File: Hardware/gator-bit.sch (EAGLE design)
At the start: 76 parts, among them J19 GATOR, J2 GATOR, J20 GATOR, J21 GATOR, J22 GATOR, J25 GATOR, J28 GATOR, J3 GATOR, J32 GATOR, J33 GATOR, J34 GATOR, J35 GATOR, J36 GATOR, J39 GATOR, J4 GATOR, J40 GATOR, U1 TPS63070, U2 micro:bit

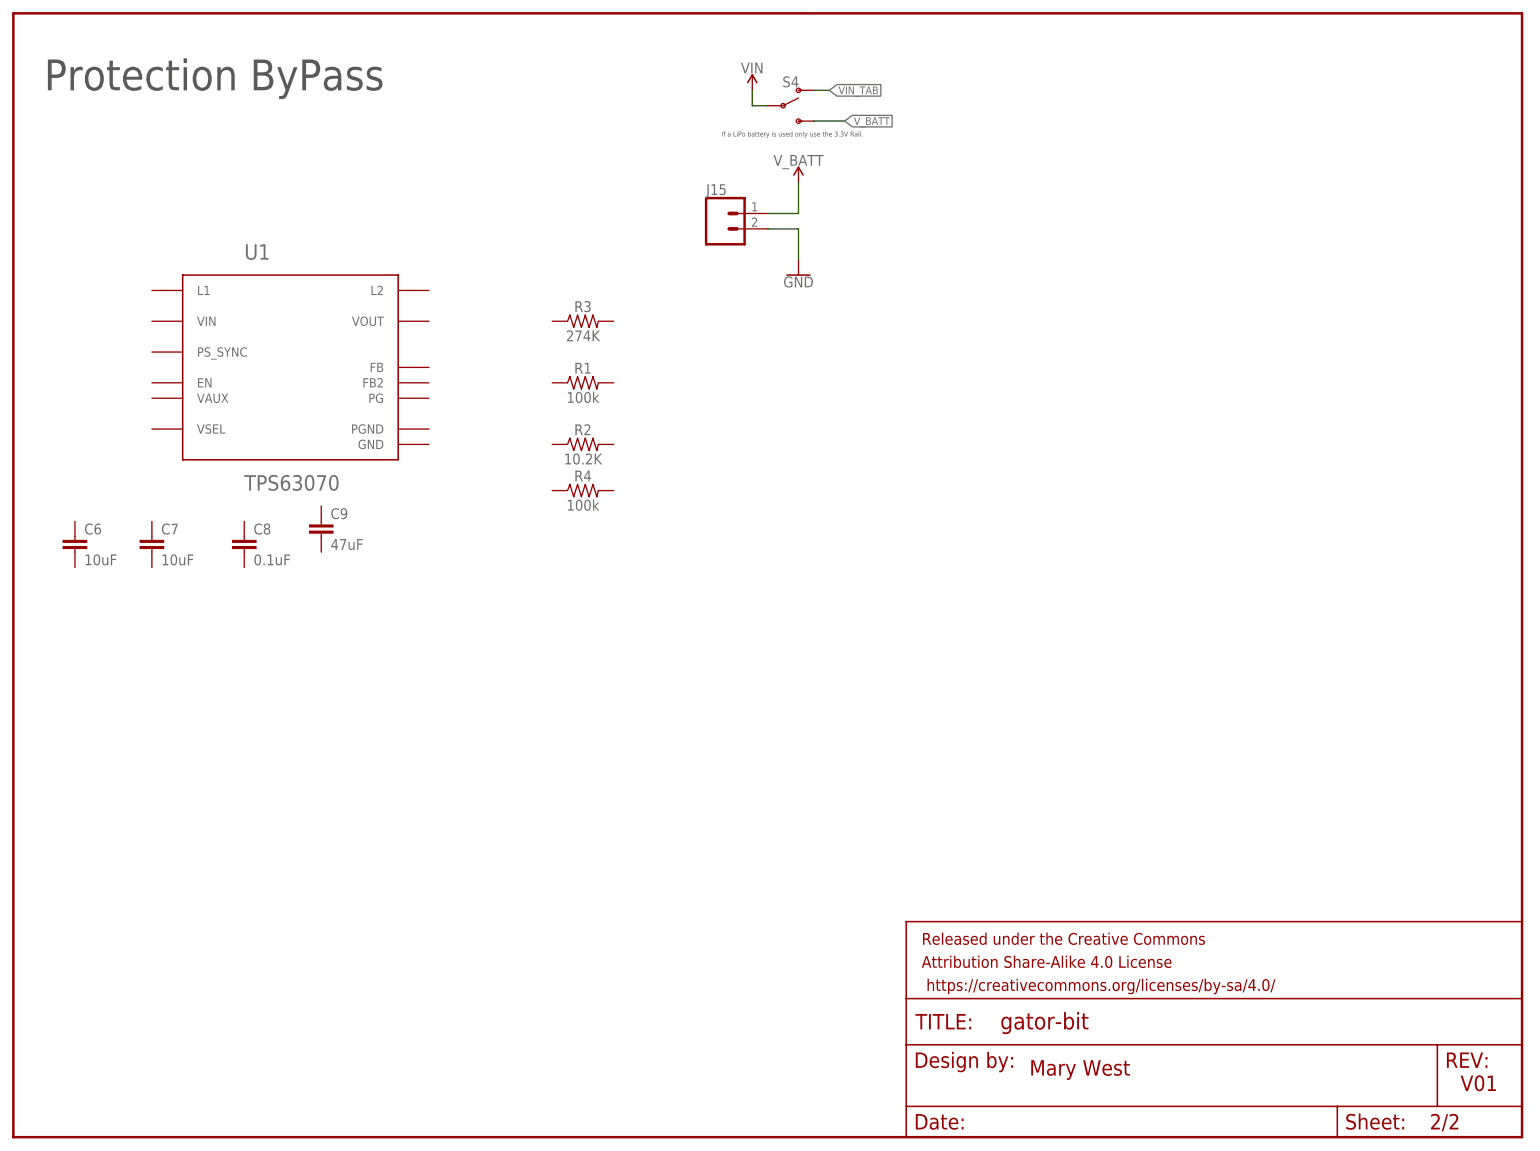
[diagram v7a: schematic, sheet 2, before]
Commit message: Added Inductor
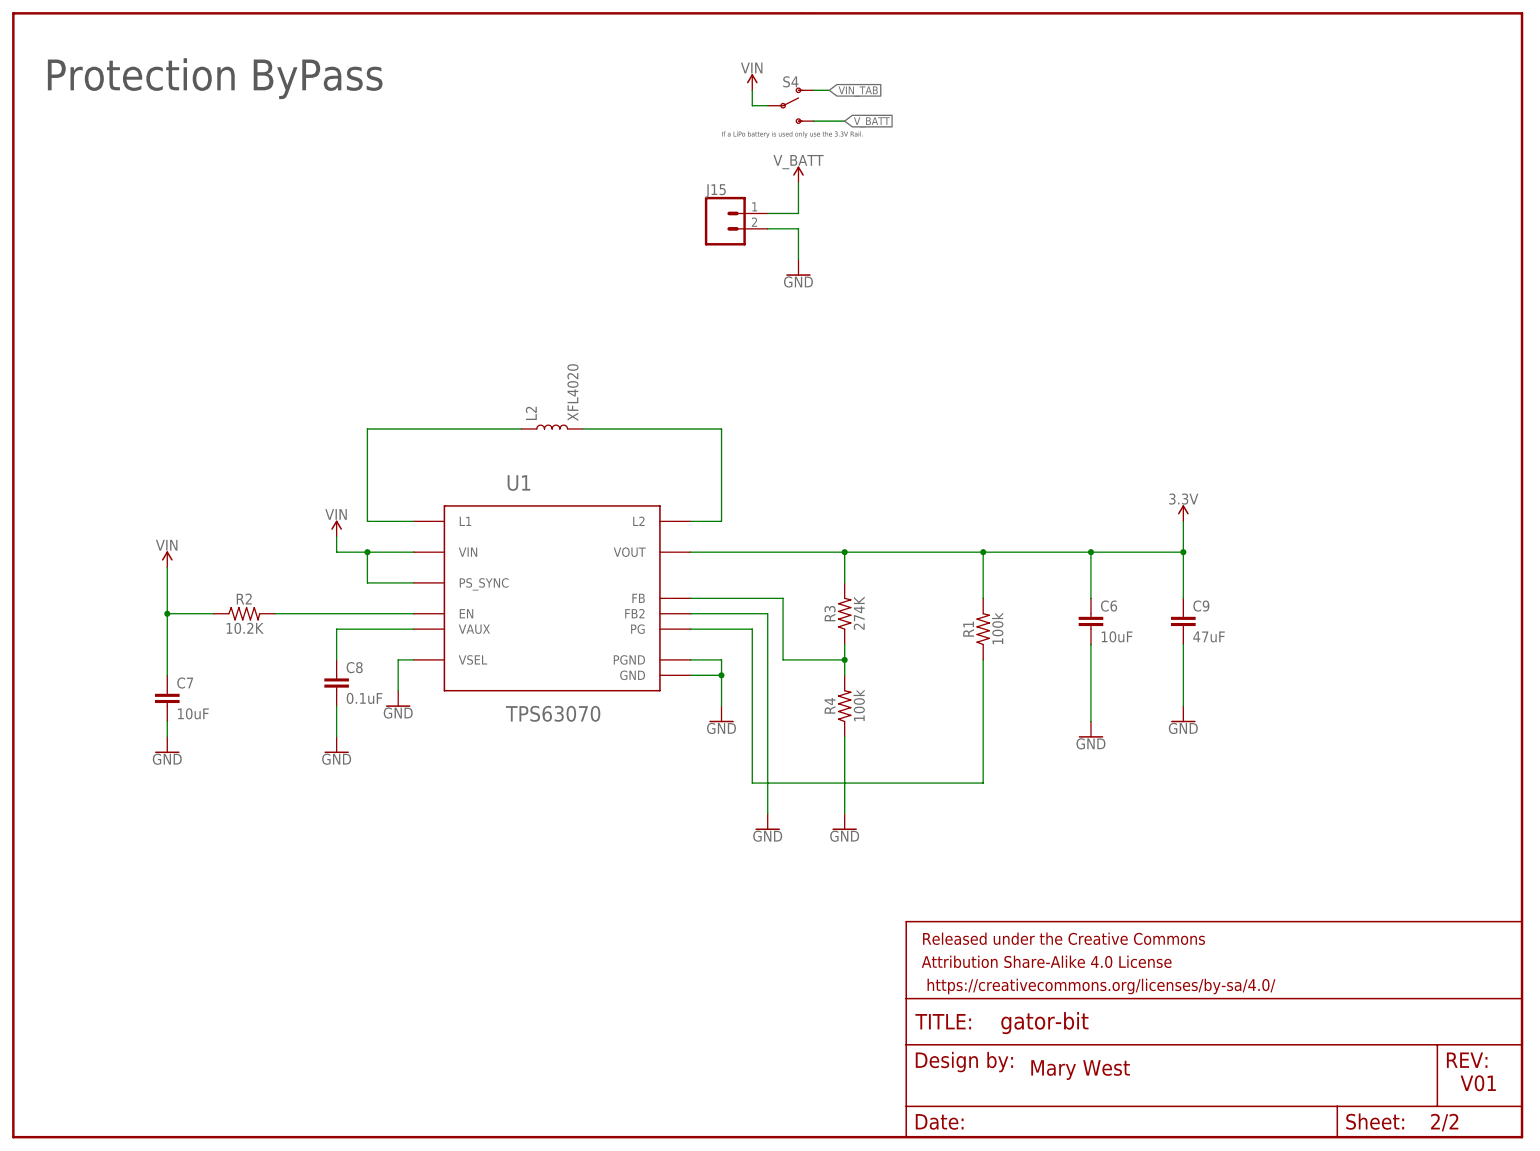
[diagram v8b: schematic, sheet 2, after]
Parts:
- added L2: XFL4020, SparkFun-Coils:XFL4020
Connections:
- new net N$11: R3.1, R4.2, U1.FB
- new net N$12: C8.1, U1.VAUX
- new net N$13: R2.2, U1.EN
- new net N$14: R1.1, U1.PG
- new net N$2: L2.1, U1.L1
- new net N$8: L2.2, U1.L2
- net 3.3V: now also C6.1, C9.1, R1.2, R3.2, U1.VOUT
- net GND: now also C6.2, C7.2, C8.2, C9.2, R4.1, U1.FB2, U1.GND, U1.PGND, U1.VSEL
- net VIN: now also C7.1, R2.1, U1.PS_SYNC, U1.VIN
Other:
- moved on the sheet: C6, C7, C8, C9, R1, R2, R3, R4, U1
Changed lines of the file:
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@@
 <part name="C8" library="SparkFun-Capacitors" deviceset="0.1UF" device="-0603-25V-(+80/-20%)" value="0.1uF"/>
 <part name="C9" library="SparkFun-Capacitors" deviceset="47UF" device="" technology="20%-6.3V-0805" value="47uF"/>
+<part name="L2" library="SparkFun-Coils" deviceset="XFL4020" device=""/>
+<part name="GND7" library="SparkFun-PowerSymbols" deviceset="GND" device=""/>
+<part name="GND8" library="SparkFun-PowerSymbols" deviceset="GND" device=""/>
+<part name="GND9" library="SparkFun-PowerSymbols" deviceset="GND" device=""/>
+<part name="SUPPLY18" library="SparkFun-PowerSymbols" deviceset="VIN" device=""/>
+<part name="SUPPLY19" library="SparkFun-PowerSymbols" deviceset="VIN" device=""/>
+<part name="GND10" library="SparkFun-PowerSymbols" deviceset="GND" device=""/>
+<part name="GND11" library="SparkFun-PowerSymbols" deviceset="GND" device=""/>
+<part name="GND17" library="SparkFun-PowerSymbols" deviceset="GND" device=""/>
+<part name="GND18" library="SparkFun-PowerSymbols" deviceset="GND" device=""/>
+<part name="GND20" library="SparkFun-PowerSymbols" deviceset="GND" device=""/>
+<part name="SUPPLY20" library="SparkFun-PowerSymbols" deviceset="3.3V" device=""/>
 </parts>
 <sheets>
@@
 <instance part="S4" gate="1" x="127" y="170.18"/>
 <instance part="SUPPLY3" gate="G$1" x="121.92" y="172.72"/>
-<instance part="U1" gate="G$1" x="45.72" y="127"/>
-<instance part="R1" gate="G$1" x="93.98" y="124.46"/>
-<instance part="R2" gate="G$1" x="93.98" y="114.3"/>
-<instance part="R3" gate="G$1" x="93.98" y="134.62"/>
-<instance part="R4" gate="G$1" x="93.98" y="106.68"/>
-<instance part="C6" gate="G$1" x="10.16" y="96.52"/>
-<instance part="C7" gate="G$1" x="22.86" y="96.52"/>
-<instance part="C8" gate="G$1" x="38.1" y="96.52"/>
-<instance part="C9" gate="G$1" x="50.8" y="99.06"/>
+<instance part="U1" gate="G$1" x="88.9" y="88.9"/>
+<instance part="R1" gate="G$1" x="160.02" y="83.82" rot="R90"/>
+<instance part="R2" gate="G$1" x="38.1" y="86.36"/>
+<instance part="R3" gate="G$1" x="137.16" y="86.36" rot="R90"/>
+<instance part="R4" gate="G$1" x="137.16" y="71.12" rot="R90"/>
+<instance part="C6" gate="G$1" x="177.8" y="83.82"/>
+<instance part="C7" gate="G$1" x="25.4" y="71.12"/>
+<instance part="C8" gate="G$1" x="53.34" y="73.66"/>
+<instance part="C9" gate="G$1" x="193.04" y="83.82"/>
+<instance part="L2" gate="G$1" x="88.9" y="116.84" rot="R90"/>
+<instance part="GND7" gate="1" x="53.34" y="63.5"/>
+<instance part="GND8" gate="1" x="25.4" y="63.5"/>
+<instance part="GND9" gate="1" x="63.5" y="71.12"/>
+<instance part="SUPPLY18" gate="G$1" x="53.34" y="99.06"/>
+<instance part="SUPPLY19" gate="G$1" x="25.4" y="93.98"/>
+<instance part="GND10" gate="1" x="116.84" y="68.58"/>
+<instance part="GND11" gate="1" x="137.16" y="50.8"/>
+<instance part="GND17" gate="1" x="124.46" y="50.8"/>
+<instance part="GND18" gate="1" x="177.8" y="66.04"/>
+<instance part="GND20" gate="1" x="193.04" y="68.58"/>
+<instance part="SUPPLY20" gate="G$1" x="193.04" y="101.6"/>
 </instances>
 <busses>
@@
 <pinref part="GND26" gate="1" pin="GND"/>
 </segment>
+<segment>
+<pinref part="C8" gate="G$1" pin="2"/>
+<wire x1="53.34" y1="71.12" x2="53.34" y2="66.04" width="0.1524" layer="91"/>
+<pinref part="GND7" gate="1" pin="GND"/>
+</segment>
+<segment>
+<pinref part="C7" gate="G$1" pin="2"/>
+<wire x1="25.4" y1="68.58" x2="25.4" y2="66.04" width="0.1524" layer="91"/>
+<pinref part="GND8" gate="1" pin="GND"/>
+</segment>
+<segment>
+<pinref part="U1" gate="G$1" pin="VSEL"/>
+<wire x1="66.04" y1="78.74" x2="63.5" y2="78.74" width="0.1524" layer="91"/>
+<wire x1="63.5" y1="78.74" x2="63.5" y2="73.66" width="0.1524" layer="91"/>
+<pinref part="GND9" gate="1" pin="GND"/>
+</segment>
+<segment>
+<pinref part="U1" gate="G$1" pin="PGND"/>
+<wire x1="111.76" y1="78.74" x2="116.84" y2="78.74" width="0.1524" layer="91"/>
+<wire x1="116.84" y1="78.74" x2="116.84" y2="76.2" width="0.1524" layer="91"/>
+<pinref part="U1" gate="G$1" pin="GND"/>
+<wire x1="116.84" y1="76.2" x2="116.84" y2="71.12" width="0.1524" layer="91"/>
+<wire x1="111.76" y1="76.2" x2="116.84" y2="76.2" width="0.1524" layer="91"/>
+<pinref part="GND10" gate="1" pin="GND"/>
+<junction x="116.84" y="76.2"/>
+</segment>
+<segment>
+<pinref part="R4" gate="G$1" pin="1"/>
+<wire x1="137.16" y1="66.04" x2="137.16" y2="53.34" width="0.1524" layer="91"/>
+<pinref part="GND11" gate="1" pin="GND"/>
+</segment>
+<segment>
+<pinref part="U1" gate="G$1" pin="FB2"/>
+<wire x1="111.76" y1="86.36" x2="124.46" y2="86.36" width="0.1524" layer="91"/>
+<wire x1="124.46" y1="86.36" x2="124.46" y2="53.34" width="0.1524" layer="91"/>
+<pinref part="GND17" gate="1" pin="GND"/>
+</segment>
+<segment>
+<pinref part="C6" gate="G$1" pin="2"/>
+<wire x1="177.8" y1="81.28" x2="177.8" y2="68.58" width="0.1524" layer="91"/>
+<pinref part="GND18" gate="1" pin="GND"/>
+</segment>
+<segment>
+<pinref part="C9" gate="G$1" pin="2"/>
+<wire x1="193.04" y1="81.28" x2="193.04" y2="71.12" width="0.1524" layer="91"/>
+<pinref part="GND20" gate="1" pin="GND"/>
+</segment>
 </net>
 <net name="V_BATT" class="0">
@@
 <pinref part="SUPPLY3" gate="G$1" pin="VIN"/>
 </segment>
-</net>
+<segment>
+<pinref part="U1" gate="G$1" pin="VIN"/>
+<wire x1="66.04" y1="96.52" x2="58.42" y2="96.52" width="0.1524" layer="91"/>
+<wire x1="58.42" y1="96.52" x2="53.34" y2="96.52" width="0.1524" layer="91"/>
+<wire x1="53.34" y1="96.52" x2="53.34" y2="99.06" width="0.1524" layer="91"/>
+<pinref part="U1" gate="G$1" pin="PS_SYNC"/>
+<wire x1="66.04" y1="91.44" x2="58.42" y2="91.44" width="0.1524" layer="91"/>
+<wire x1="58.42" y1="91.44" x2="58.42" y2="96.52" width="0.1524" layer="91"/>
+<junction x="58.42" y="96.52"/>
+<pinref part="SUPPLY18" gate="G$1" pin="VIN"/>
+</segment>
+<segment>
+<pinref part="R2" gate="G$1" pin="1"/>
+<wire x1="33.02" y1="86.36" x2="25.4" y2="86.36" width="0.1524" layer="91"/>
+<wire x1="25.4" y1="86.36" x2="25.4" y2="93.98" width="0.1524" layer="91"/>
+<pinref part="C7" gate="G$1" pin="1"/>
+<wire x1="25.4" y1="86.36" x2="25.4" y2="76.2" width="0.1524" layer="91"/>
+<junction x="25.4" y="86.36"/>
+<pinref part="SUPPLY19" gate="G$1" pin="VIN"/>
+</segment>
+</net>
+<net name="N$2" class="0">
+<segment>
+<pinref part="L2" gate="G$1" pin="1"/>
+<wire x1="83.82" y1="116.84" x2="58.42" y2="116.84" width="0.1524" layer="91"/>
+<wire x1="58.42" y1="116.84" x2="58.42" y2="101.6" width="0.1524" layer="91"/>
+<pinref part="U1" gate="G$1" pin="L1"/>
+<wire x1="58.42" y1="101.6" x2="66.04" y2="101.6" width="0.1524" layer="91"/>
+</segment>
+</net>
+<net name="N$8" class="0">
+<segment>
+<pinref part="L2" gate="G$1" pin="2"/>
+<wire x1="93.98" y1="116.84" x2="116.84" y2="116.84" width="0.1524" layer="91"/>
+<wire x1="116.84" y1="116.84" x2="116.84" y2="101.6" width="0.1524" layer="91"/>
+<pinref part="U1" gate="G$1" pin="L2"/>
+<wire x1="116.84" y1="101.6" x2="111.76" y2="101.6" width="0.1524" layer="91"/>
+</segment>
+</net>
+<net name="N$13" class="0">
+<segment>
+<pinref part="R2" gate="G$1" pin="2"/>
+<wire x1="66.04" y1="86.36" x2="43.18" y2="86.36" width="0.1524" layer="91"/>
+<pinref part="U1" gate="G$1" pin="EN"/>
+</segment>
+</net>
+<net name="N$12" class="0">
+<segment>
+<pinref part="U1" gate="G$1" pin="VAUX"/>
+<wire x1="66.04" y1="83.82" x2="53.34" y2="83.82" width="0.1524" layer="91"/>
+<pinref part="C8" gate="G$1" pin="1"/>
+<wire x1="53.34" y1="83.82" x2="53.34" y2="78.74" width="0.1524" layer="91"/>
+</segment>
+</net>
+<net name="N$11" class="0">
+<segment>
+<pinref part="R3" gate="G$1" pin="1"/>
+<pinref part="R4" gate="G$1" pin="2"/>
+<wire x1="137.16" y1="81.28" x2="137.16" y2="78.74" width="0.1524" layer="91"/>
+<pinref part="U1" gate="G$1" pin="FB"/>
+<wire x1="137.16" y1="78.74" x2="137.16" y2="76.2" width="0.1524" layer="91"/>
+<wire x1="111.76" y1="88.9" x2="127" y2="88.9" width="0.1524" layer="91"/>
+<wire x1="127" y1="88.9" x2="127" y2="78.74" width="0.1524" layer="91"/>
+<wire x1="127" y1="78.74" x2="137.16" y2="78.74" width="0.1524" layer="91"/>
+<junction x="137.16" y="78.74"/>
+</segment>
+</net>
+<net name="N$14" class="0">
+<segment>
+<pinref part="R1" gate="G$1" pin="1"/>
+<wire x1="160.02" y1="78.74" x2="160.02" y2="58.42" width="0.1524" layer="91"/>
+<wire x1="160.02" y1="58.42" x2="121.92" y2="58.42" width="0.1524" layer="91"/>
+<wire x1="121.92" y1="58.42" x2="121.92" y2="83.82" width="0.1524" layer="91"/>
+<pinref part="U1" gate="G$1" pin="PG"/>
+<wire x1="121.92" y1="83.82" x2="111.76" y2="83.82" width="0.1524" layer="91"/>
+</segment>
+</net>
+<net name="3.3V" class="0">
+<segment>
+<pinref part="U1" gate="G$1" pin="VOUT"/>
+<wire x1="111.76" y1="96.52" x2="137.16" y2="96.52" width="0.1524" layer="91"/>
+<pinref part="C9" gate="G$1" pin="1"/>
+<wire x1="137.16" y1="96.52" x2="160.02" y2="96.52" width="0.1524" layer="91"/>
+<wire x1="160.02" y1="96.52" x2="177.8" y2="96.52" width="0.1524" layer="91"/>
+<wire x1="177.8" y1="96.52" x2="193.04" y2="96.52" width="0.1524" layer="91"/>
+<wire x1="193.04" y1="96.52" x2="193.04" y2="88.9" width="0.1524" layer="91"/>
+<pinref part="C6" gate="G$1" pin="1"/>
+<wire x1="177.8" y1="88.9" x2="177.8" y2="96.52" width="0.1524" layer="91"/>
+<pinref part="R1" gate="G$1" pin="2"/>
+<wire x1="160.02" y1="88.9" x2="160.02" y2="96.52" width="0.1524" layer="91"/>
+<pinref part="R3" gate="G$1" pin="2"/>
+<wire x1="137.16" y1="91.44" x2="137.16" y2="96.52" width="0.1524" layer="91"/>
+<junction x="137.16" y="96.52"/>
+<junction x="160.02" y="96.52"/>
+<junction x="177.8" y="96.52"/>
+<pinref part="SUPPLY20" gate="G$1" pin="3.3V"/>
+<wire x1="193.04" y1="96.52" x2="193.04" y2="101.6" width="0.1524" layer="91"/>
+<junction x="193.04" y="96.52"/>
+</segment>
+</net>
